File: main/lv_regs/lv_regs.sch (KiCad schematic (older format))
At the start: 23 parts, among them J1 Output

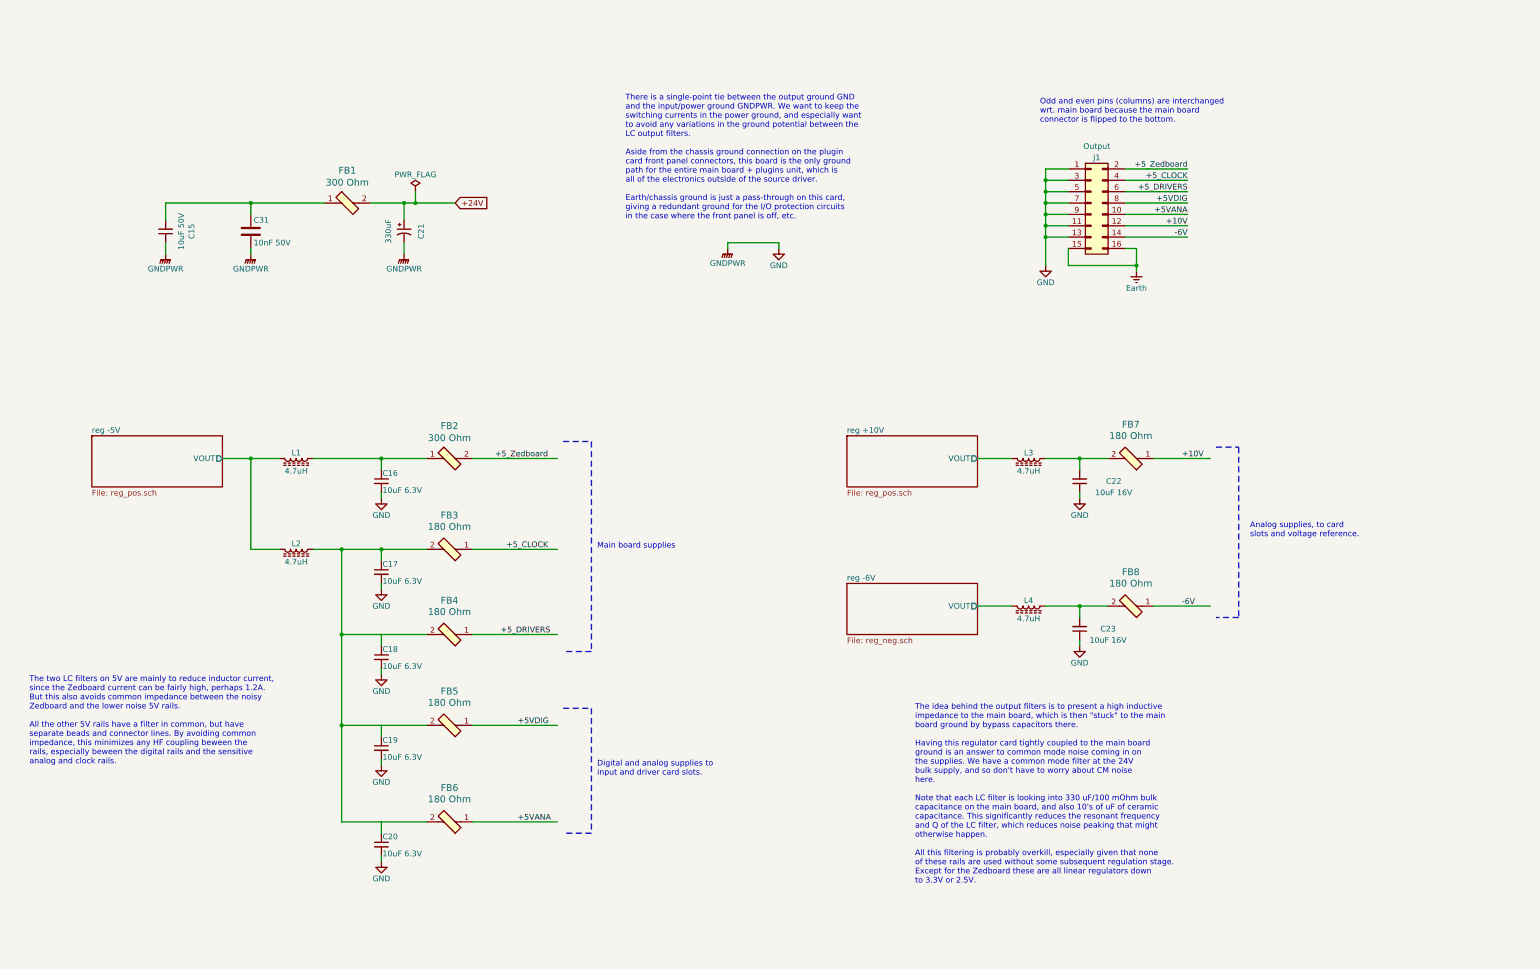
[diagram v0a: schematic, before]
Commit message: A near final version of the low-volt regulator board. Pending footprint comparison on the actual parts.
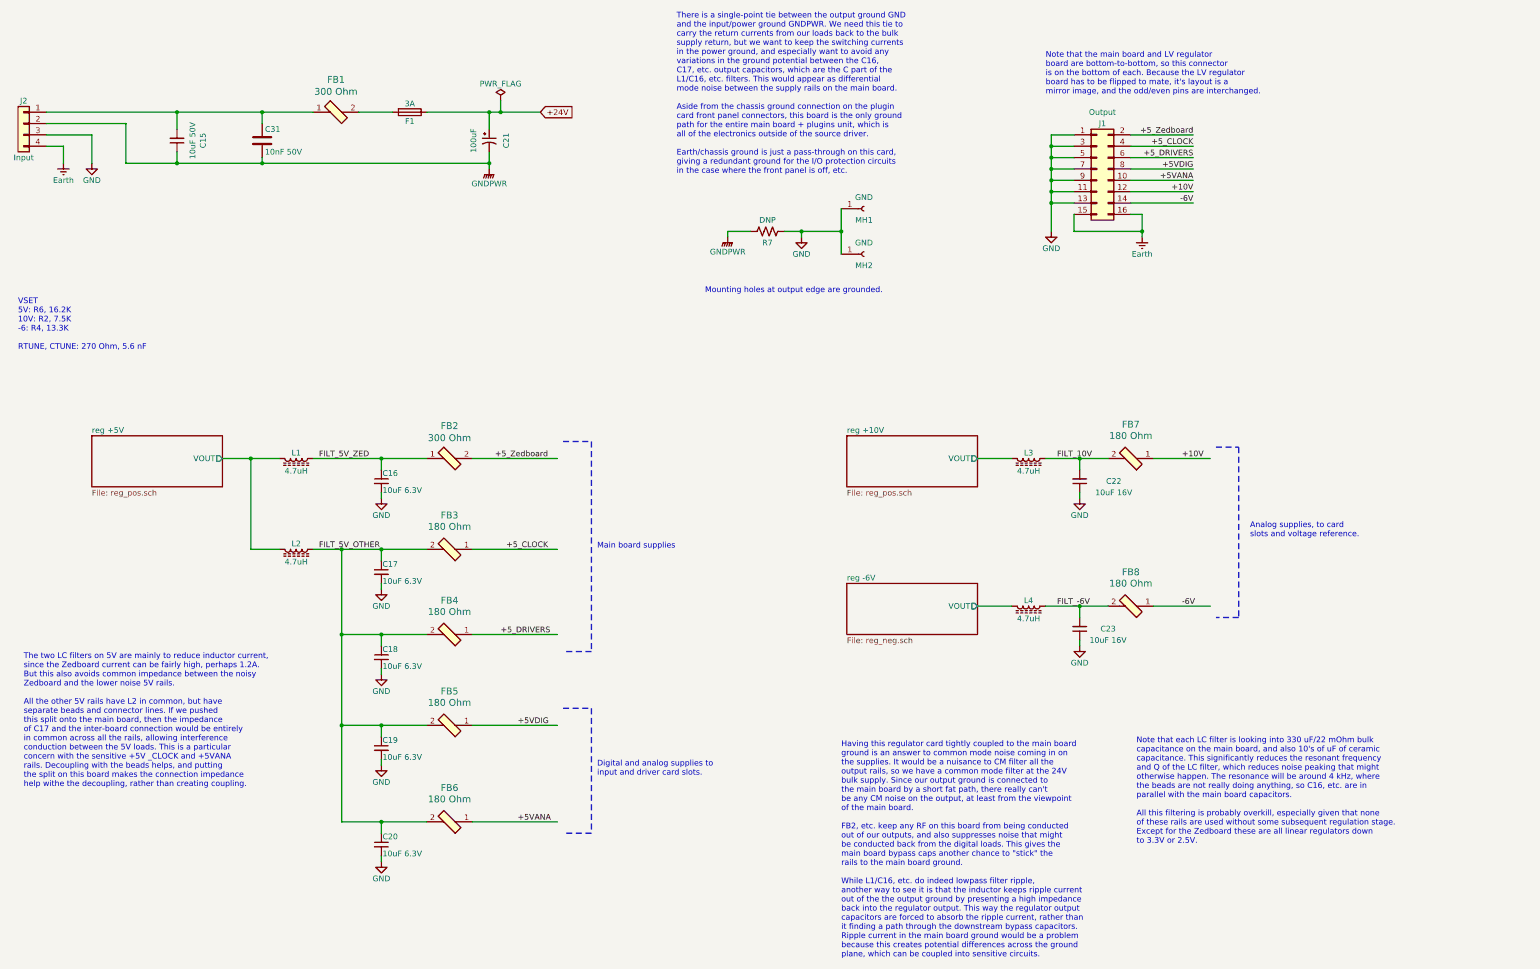
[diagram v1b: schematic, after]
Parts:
- added F1: 3A, Fuse:Fuseholder_Cylinder-5x20mm_Schurter_0031_8201_Horizontal_Open, symbol Device:Fuse
- added J2: Input, Connector_Molex:Molex_Mini-Fit_Jr_5566-04A_2x02_P4.20mm_Vertical, symbol Connector_Generic:Conn_01x04
- added MH1, MH2: GND, MountingHole:MountingHole_3.2mm_M3_Pad, symbol Connector:Conn_01x01_Female
- added R7: DNP, Resistor_SMD:R_2816_7142Metric, symbol Device:R_US
- C15: DK line (none) -> P.4
- C16, C17, C18, C19, C20: DK line 20 -> M.20
- C21: value 330uF -> 100uF; DK line 21 -> P.6; Description 16V aluminum solid polymer, ESR 22 mOhm -> CAP ALUM HYBRD 100UF 20% 35V SMD; Digikey 565-4285-1-ND -> 565-HHXD350ARA101MHA0GCT-ND; MPN APXG160ARA331MH70G -> HHXD350ARA101MHA0G
- C22, C23: DK line 10 -> M.10
- C31: DK line (none) -> P.5
- FB1, FB2: DK line 13 -> M.13
- FB3, FB4, FB5, FB6, FB7, FB8: DK line 36 -> M.36
- J1: DK line (none) -> P.7; Description (none) -> CONN RCPT 16POS 0.1 GOLD PCB; Digikey (none) -> SAM1214-08-ND; MPN (none) -> SSW-108-02-G-D; Manufacturer (none) -> Samtec Inc.
- L1, L2, L3, L4: DK line (none) -> P.3
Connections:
- net labels added: FILT_-6V, FILT_10V, FILT_5V_OTHER, FILT_5V_ZED
- wire segments 83 -> 102
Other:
- note added: "Having this regulator card tightly coupled to the main board \nground is an answer to common mode noise coming in on \nthe supplies. It would be a nuisance to CM filter all the\noutput rails, so we have a common mode filter at the 24V \nbulk supply. Since our output ground is connected to\nthe main board by a short fat path, there really can't\nbe any CM noise on the output, at least from the vie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"
- note added: "Mounting holes at output edge are grounded."
- note added: "Note that each LC filter is looking into 330 uF/22 mOhm bulk\ncapacitance on the main board, and also 10's of uF of ceramic\ncapacitance. This significantly reduces the resonant frequency \nand Q of the LC filter, which reduces noise peaking that might\notherwise happen. The resonance will be around 4 kHz, where\nthe beads are not really doing anything, so C16, etc. are in \nparallel with the mai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"
- note added: "Note that the main board and LV regulator \nboard are bottom-to-bottom, so this connector \nis on the bottom of each. Because the LV regulator\nboard has to be flipped to mate, it's layout is a\nmirror image, and the odd/even pins are interchanged.\n"
- note added: "The two LC filters on 5V are mainly to reduce inductor current,\nsince the Zedboard current can be fairly high, perhaps 1.2A.\nBut this also avoids common impedance between the noisy \nZedboard and the lower noise 5V rails.\n\nAll the other 5V rails have L2 in common, but have\nseparate beads and connector lines. If we pushed \nthis split onto the main board, then the impedance\nof C17 and the in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"
- note added: "There is a single-point tie between the output ground GND\nand the input/power ground GNDPWR. We need this tie to\ncarry the return currents from our loads back to the bulk\nsupply return, but we want to keep the switching currents\nin the power ground, and especially want to avoid any\nvariations in the ground potential between the C16,\nC17, etc. output capacitors, which are the C part of the \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"
- note added: "VSET\n5V: R6, 16.2K\n10V: R2, 7.5K\n-6: R4, 13.3K\n\nRTUNE, CTUNE: 270 Ohm, 5.6 nF\n"
- note removed: "Odd and even pins (columns) are interchanged\nwrt. main board because the main board \nconnector is flipped to the bottom."
- note removed: "The idea behind the output filters is to present a high inductive \nimpedance to the main board, which is then "stuck" to the main\nboard ground by bypass capacitors there. \n\nHaving this regulator card tightly coupled to the main board \nground is an answer to common mode noise coming in on \nthe supplies. We have a common mode filter at the 24V \nbulk supply, and so don't have to worry about C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"
- note removed: "The two LC filters on 5V are mainly to reduce inductor current,\nsince the Zedboard current can be fairly high, perhaps 1.2A.\nBut this also avoids common impedance between the noisy \nZedboard and the lower noise 5V rails.\n\nAll the other 5V rails have a filter in common, but have\nseparate beads and connector lines. By avoiding common\nimpedance, this minimizes any HF coupling beween the\nrail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"
- note removed: "There is a single-point tie between the output ground GND\nand the input/power ground GNDPWR. We want to keep the\nswitching currents in the power ground, and especially want\nto avoid any variations in the ground potential between the \nLC output filters.\n\nAside from the chassis ground connection on the plugin\ncard front panel connectors, this board is the only ground\npath for the entire mai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"
- moved on the sheet: C15, C21, C31, FB1, J1

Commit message: Schematic revision for DAC board, compensation tweaks in lv_regs.
Opamp +/- pins were swapped in reference_buffer.sch as side effect of the symbol change from using a dual opamp.

lv_regs files.  The compensation components were (CTUNE/RTUNE) were quite wrong, and everything oscillated like crazy. The positive regulators are fine with no compensation, and the negative regulator benefits from a bit.
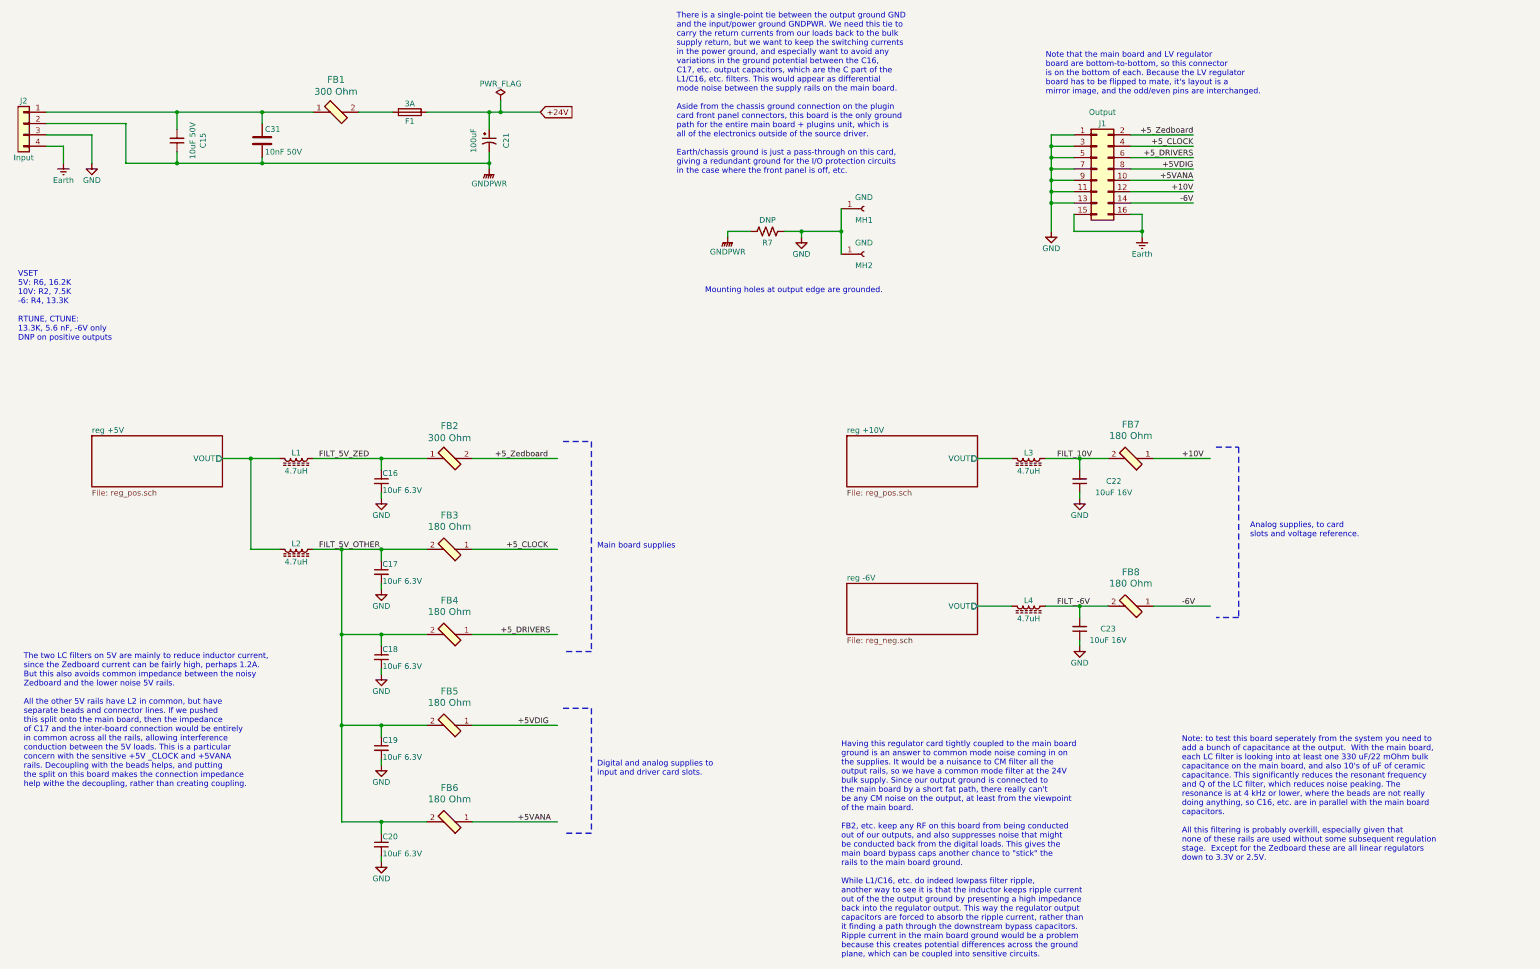
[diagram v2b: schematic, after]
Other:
- note added: "Note: to test this board seperately from the system you need to\nadd a bunch of capacitance at the output. With the main board,\neach LC filter is looking into at least one 330 uF/22 mOhm bulk\ncapacitance on the main board, and also 10's of uF of ceramic\ncapacitance. This significantly reduces the resonant frequency\nand Q of the LC filter, which reduces noise peaking. The\nresonance is at 4 kH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"
- note added: "VSET\n5V: R6, 16.2K\n10V: R2, 7.5K\n-6: R4, 13.3K\n\nRTUNE, CTUNE: \n13.3K, 5.6 nF, -6V only\nDNP on positive outputs\n\n"
- note removed: "Note that each LC filter is looking into 330 uF/22 mOhm bulk\ncapacitance on the main board, and also 10's of uF of ceramic\ncapacitance. This significantly reduces the resonant frequency \nand Q of the LC filter, which reduces noise peaking that might\notherwise happen. The resonance will be around 4 kHz, where\nthe beads are not really doing anything, so C16, etc. are in \nparallel with the mai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"
- note removed: "VSET\n5V: R6, 16.2K\n10V: R2, 7.5K\n-6: R4, 13.3K\n\nRTUNE, CTUNE: 270 Ohm, 5.6 nF\n"
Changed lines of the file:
@@
 Text Label 10850 7000 0    50   ~ 0
 FILT_-6V
-Text Notes 11550 9100 0    50   ~ 0
-Note that each LC filter is looking into 330 uF/22 mOhm bulk\ncapacitance on the main board, and also 10's of uF of ceramic\ncapacitance. This significantly reduces the resonant frequency \nand Q of the LC filter, which reduces noise peaking that might\notherwise happen. The resonance will be around 4 kHz, where\nthe beads are not really doing anything, so C16, etc. are in \nparallel with the main board capacitors.\n\nAll this filtering is probably overkill, especially given that none\nof these rails are used without some subsequent regulation stage.\nExcept for the Zedboard these are all linear regulators down\nto 3.3V or 2.5V.
+Text Notes 11950 9250 0    50   ~ 0
+Note: to test this board seperately from the system you need to\nadd a bunch of capacitance at the output.  With the main board,\neach LC filter is looking into at least one 330 uF/22 mOhm bulk\ncapacitance on the main board, and also 10's of uF of ceramic\ncapacitance. This significantly reduces the resonant frequency\nand Q of the LC filter, which reduces noise peaking. The\nresonance is at 4 kHz or lower, where the beads are not really\ndoing anything, so C16, etc. are in parallel with the main board\ncapacitors.\n\nAll this filtering is probably overkill, especially given that\nnone of these rails are used without some subsequent regulation\nstage.  Except for the Zedboard these are all linear regulators\ndown to 3.3V or 2.5V.\n
 $Comp
 L Device:Fuse F1
@@
 Connection ~ 3850 3100
 Text Notes 1700 4750 0    50   ~ 0
-VSET\n5V: R6, 16.2K\n10V: R2, 7.5K\n-6: R4, 13.3K\n\nRTUNE, CTUNE: 270 Ohm, 5.6 nF\n
+VSET\n5V: R6, 16.2K\n10V: R2, 7.5K\n-6: R4, 13.3K\n\nRTUNE, CTUNE:  \n13.3K, 5.6 nF, -6V only\nDNP on positive outputs\n\n
 $EndSCHEMATC
